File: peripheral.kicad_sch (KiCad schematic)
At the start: 24 parts, among them J17 S8411-45R, J18 10129380-902001BLF, U2 MCP7940NT-I_SN, U4 SN74LV4052ADR, U5 PCAL6524HEAZ, Y1 32.768KHZ

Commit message: Layout draft
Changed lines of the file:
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@@
 	(wire
 		(pts
-			(xy 224.79 85.09) (xy 234.95 85.09)
+			(xy 224.79 85.09) (xy 236.22 85.09)
 		)
 		(stroke
@@
 	(global_label "GNSS_RST"
 		(shape output)
-		(at 234.95 85.09 0)
+		(at 236.22 85.09 0)
 		(fields_autoplaced yes)
 		(effects
@@
 		)
 		(property "Intersheetrefs" "${INTERSHEET_REFS}"
-			(at 247.3694 85.09 0)
+			(at 248.6394 85.09 0)
 			(effects
 				(font
@@
 	)
 	(global_label "IOXP_INT"
-		(shape input)
+		(shape output)
 		(at 182.88 64.77 180)
 		(fields_autoplaced yes)
@@
 			)
 		)
-		(property "Description" "IC, SWITCH, 4:1"
+		(property "Description" "IC, MUX, 4:1"
 			(at 66.04 62.23 0)
 			(effects

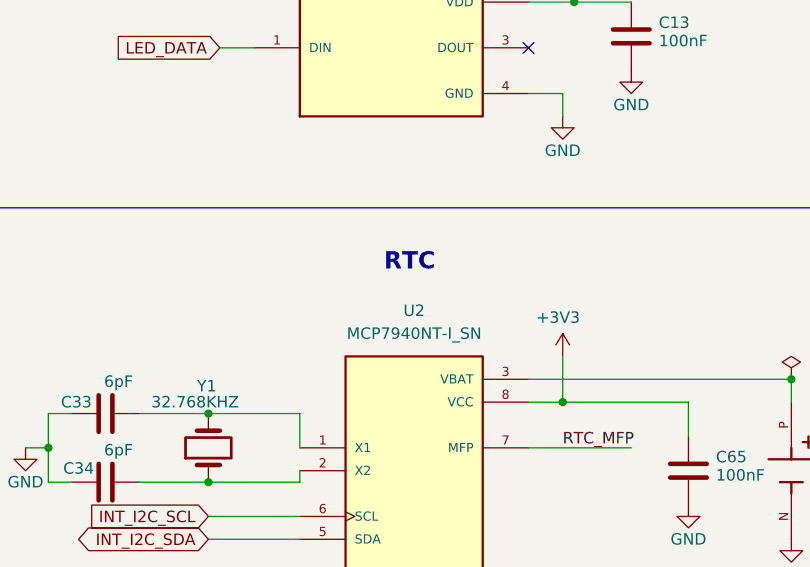
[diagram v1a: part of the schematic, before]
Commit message: More mfg readiness tweaks; ext power hdr
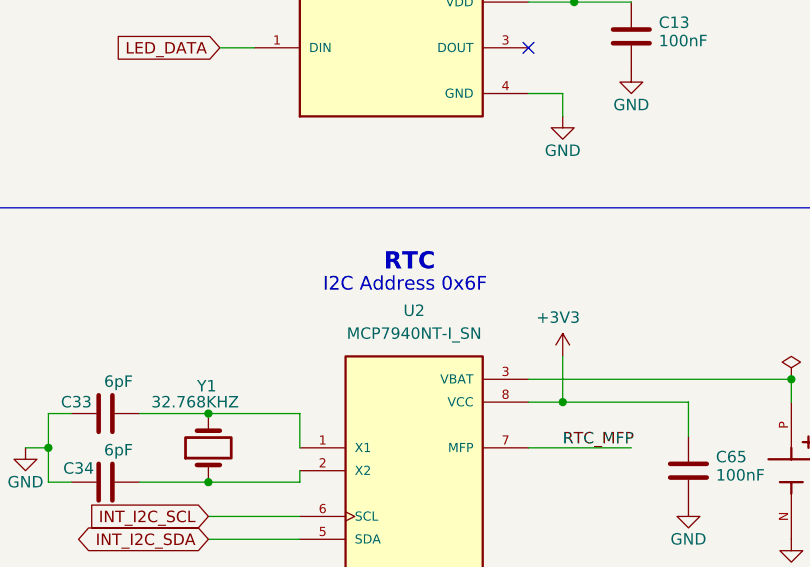
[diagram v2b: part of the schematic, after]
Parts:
- TP12, TP13, TP14, TP15: now left out of the parts list
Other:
- note added: "I2C Address 0x6F"
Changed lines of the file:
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@@
 	(title_block
 		(title "TELLUS Networked Sensor Solutions, Inc. ")
-		(date "2025-09-16")
+		(date "2025-10-28")
 		(rev "v1.0.0")
 	)
@@
 		)
 	)
+	(text "I2C Address 0x6F"
+		(exclude_from_sim no)
+		(at 70.104 144.526 0)
+		(effects
+			(font
+				(size 1.524 1.524)
+			)
+		)
+	)
 	(label "HW_ID2"
 		(at 231.14 74.93 0)
@@
 		(unit 1)
 		(exclude_from_sim no)
-		(in_bom yes)
+		(in_bom no)
 		(on_board yes)
 		(dnp no)
@@
 		(unit 1)
 		(exclude_from_sim no)
-		(in_bom yes)
+		(in_bom no)
 		(on_board yes)
 		(dnp no)
@@
 		(unit 1)
 		(exclude_from_sim no)
-		(in_bom yes)
+		(in_bom no)
 		(on_board yes)
 		(dnp no)
@@
 		(unit 1)
 		(exclude_from_sim no)
-		(in_bom yes)
+		(in_bom no)
 		(on_board yes)
 		(dnp no)
